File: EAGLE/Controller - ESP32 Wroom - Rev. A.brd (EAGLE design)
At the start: 29.5 x 33 mm, 30 parts, among them IC1 ESP32-S3-WROOM-1-N8R2, IC2 MPM3610GQV-P, IC3 CP2102N-A02-GQFN20R, J1 DF12NB_4.0_-40DP-0.5V_51_, J4 FSI-105-03-X-S, J8 -

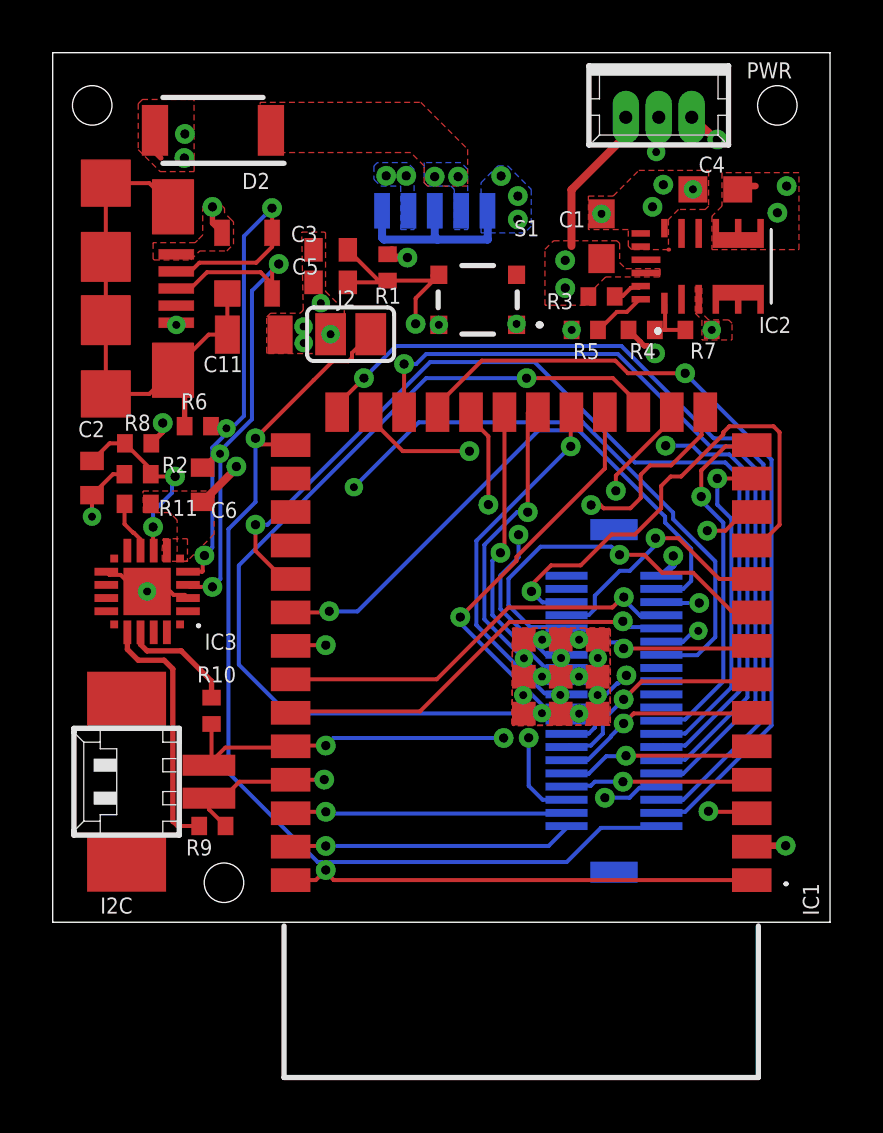
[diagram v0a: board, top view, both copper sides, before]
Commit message: Fixed some clearance error
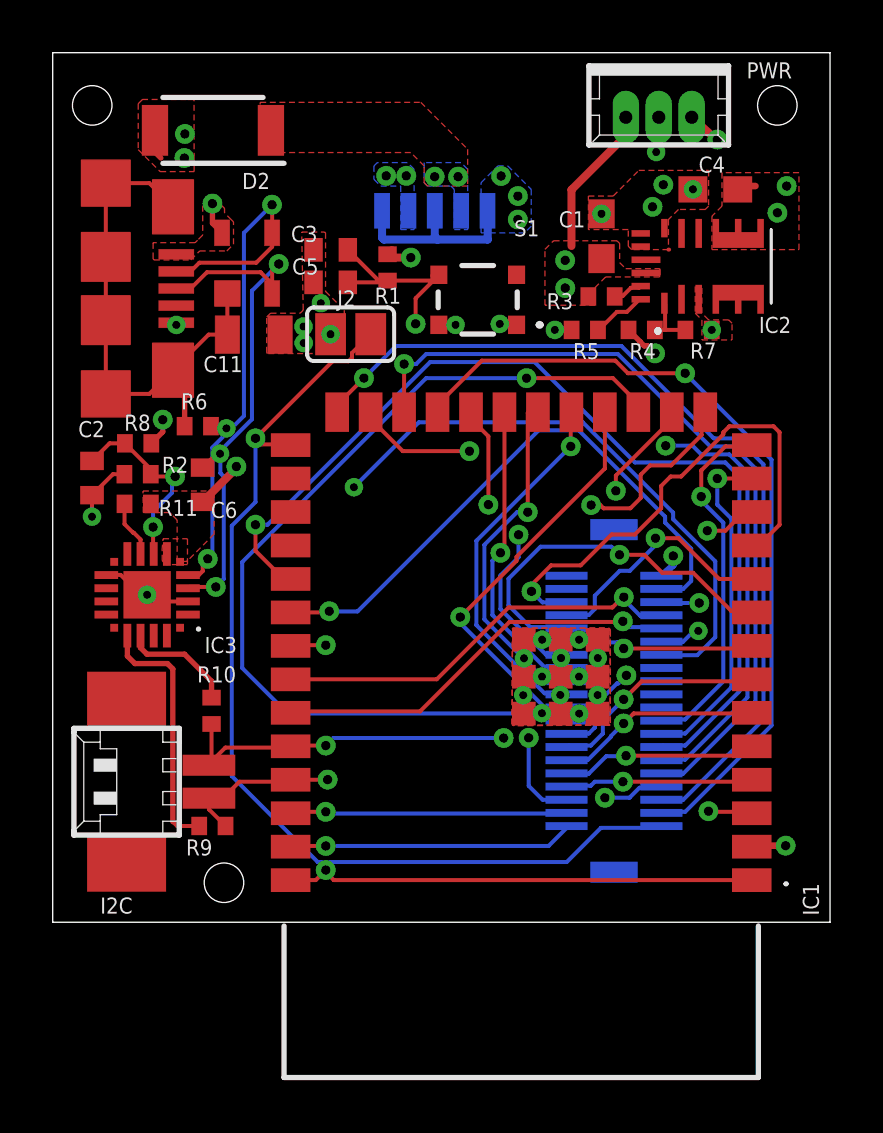
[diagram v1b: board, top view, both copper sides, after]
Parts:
- moved IC3 0.13 mm to (3.58, 12.4)
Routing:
- net GND: track 37.2 -> 39.0 mm

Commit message: Changed some via to be passthrought
Added schematic and new board layout prints
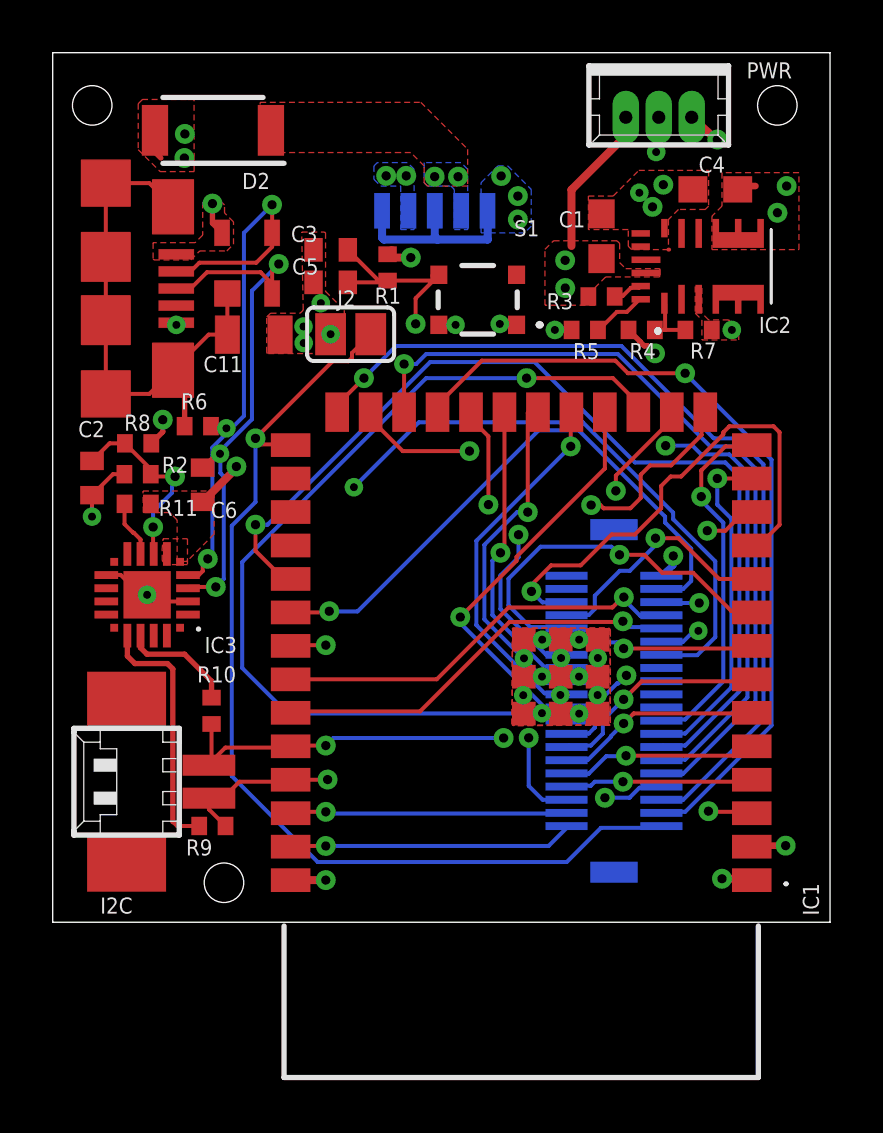
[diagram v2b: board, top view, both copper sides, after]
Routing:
- net GND: track 39.0 -> 23.7 mm
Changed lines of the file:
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@@
 <layer number="13" name="Route13" color="4" fill="5" visible="no" active="no"/>
 <layer number="14" name="Route14" color="1" fill="6" visible="no" active="no"/>
-<layer number="15" name="Route15" color="4" fill="6" visible="yes" active="yes"/>
+<layer number="15" name="Route15" color="4" fill="6" visible="no" active="yes"/>
 <layer number="16" name="Bottom" color="1" fill="1" visible="yes" active="yes"/>
 <layer number="17" name="Pads" color="2" fill="1" visible="yes" active="yes"/>
@@
 <layer number="43" name="vRestrict" color="2" fill="10" visible="no" active="yes"/>
 <layer number="44" name="Drills" color="7" fill="1" visible="no" active="yes"/>
-<layer number="45" name="Holes" color="7" fill="1" visible="yes" active="yes"/>
+<layer number="45" name="Holes" color="7" fill="1" visible="no" active="yes"/>
 <layer number="46" name="Milling" color="3" fill="1" visible="no" active="yes"/>
 <layer number="47" name="Measures" color="7" fill="1" visible="no" active="yes"/>
@@
 <param name="layerSetup" value="([2:1+(2*15)+16:15])"/>
 <param name="mtCopper" value="0.035mm 0.035mm 0.035mm 0.035mm 0.035mm 0.035mm 0.035mm 0.035mm 0.035mm 0.035mm 0.035mm 0.035mm 0.035mm 0.035mm 0.035mm 0.035mm"/>
-<param name="mtIsolate" value="0.11mm 1.6mm 0.2mm 0.15mm 0.2mm 0.15mm 0.2mm 0.15mm 0.2mm 0.15mm 0.2mm 0.15mm 0.2mm 0.15mm 0.11mm"/>
+<param name="mtIsolate" value="0.11mm 0.8mm 0.2mm 0.15mm 0.2mm 0.15mm 0.2mm 0.15mm 0.2mm 0.15mm 0.2mm 0.15mm 0.2mm 0.15mm 0.11mm"/>
 <param name="mdWireWire" value="6mil"/>
 <param name="mdWirePad" value="6mil"/>
@@
 <vertex x="24.638" y="22.86"/>
 <vertex x="24.638" y="22.098"/>
-<vertex x="25.781" y="22.098"/>
-<vertex x="25.781" y="22.733"/>
+<vertex x="26.035" y="22.098"/>
+<vertex x="26.035" y="22.479"/>
 <vertex x="25.654" y="22.86"/>
 <vertex x="24.892" y="22.86"/>
@@
 <wire x1="17.907" y1="10.5918" x2="17.88" y2="10.718" width="0.1524" layer="1"/>
 <wire x1="17.6784" y1="22.6314" x2="17.604" y2="22.672" width="0.1524" layer="1"/>
-<wire x1="9.9822" y1="1.6002" x2="9.0678" y2="1.6002" width="0.1524" layer="1"/>
-<wire x1="10.3632" y1="1.9812" x2="9.9822" y2="1.6002" width="0.1524" layer="1"/>
+<wire x1="10.3632" y1="1.6002" x2="9.0678" y2="1.6002" width="0.3048" layer="1"/>
 <wire x1="9.0678" y1="1.6002" x2="9.03" y2="1.598" width="0.1524" layer="1"/>
-<wire x1="10.668" y1="1.6002" x2="26.5176" y2="1.6002" width="0.1524" layer="1"/>
-<wire x1="10.3632" y1="1.905" x2="10.668" y2="1.6002" width="0.1524" layer="1"/>
-<wire x1="26.5176" y1="1.6002" x2="26.53" y2="1.598" width="0.1524" layer="1"/>
-<wire x1="10.3632" y1="1.905" x2="10.3632" y2="1.9812" width="0.1524" layer="1"/>
+<wire x1="26.53" y1="1.598" x2="26.5176" y2="1.6002" width="0.1524" layer="1"/>
+<wire x1="10.3632" y1="1.524" x2="10.3632" y2="1.6002" width="0.1524" layer="1"/>
 <wire x1="23.3934" y1="25.527" x2="23.368" y2="25.527" width="0.1524" layer="1"/>
-<via x="10.3632" y="1.9812" extent="1-2" drill="0.35"/>
+<via x="10.3632" y="1.6002" extent="1-16" drill="0.35"/>
 <wire x1="23.1" y1="13.15" x2="23.550659375" y2="13.546659375" width="0.254" layer="16"/>
 <wire x1="23.550659375" y1="13.546659375" x2="23.55064375" y2="13.90326875" width="0.254" layer="16"/>
@@
 <wire x1="17.88" y1="9.318" x2="17.8854" y2="9.318" width="0.254" layer="1"/>
 <wire x1="17.8854" y1="9.318" x2="17.907" y2="9.2964" width="0.254" layer="1"/>
-<via x="20.828" y="26.885" extent="1-2" drill="0.3" diameter="0.1778"/>
-<via x="24.296" y="27.813" extent="1-2" drill="0.3" diameter="0.1778"/>
+<via x="22.264" y="27.686" extent="1-2" drill="0.3" diameter="0.1778"/>
 <contactref element="PWR" pad="2"/>
 <wire x1="17.88" y1="10.718" x2="18.57040625" y2="10.718" width="0.1524" layer="1"/>
@@
 <via x="19.058" y="22.479" extent="1-2" drill="0.3"/>
 <via x="15.289" y="22.672" extent="1-2" drill="0.3"/>
-<via x="25.011" y="22.479" extent="1-2" drill="0.3"/>
+<via x="25.773" y="22.479" extent="1-2" drill="0.3"/>
 <wire x1="1.4915875" y1="16.2084875" x2="1.4915875" y2="15.393696875" width="0.1524" layer="1"/>
 <wire x1="1.4915875" y1="15.393696875" x2="1.4917625" y2="15.393521875" width="0.1524" layer="1"/>
@@
 <wire x1="14.654" y1="22.672" x2="15.289" y2="22.672" width="0.254" layer="1"/>
 <wire x1="19.693" y1="22.479" x2="19.058" y2="22.479" width="0.254" layer="1"/>
+<via x="25.4" y="1.651" extent="1-16" drill="0.35"/>
+<wire x1="26.5176" y1="1.6002" x2="26.4668" y2="1.651" width="0.3048" layer="1"/>
+<wire x1="26.4668" y1="1.651" x2="25.4" y2="1.651" width="0.3048" layer="1"/>
 </signal>
 <signal name="+3V3" class="2">
@@
 <via x="6.062571875" y="27.274003125" extent="1-16" drill="0.35"/>
 <polygon width="0.2032" layer="1" thermals="no">
-<vertex x="3.81" y="25.4"/>
+<vertex x="3.81" y="25.7817375"/>
 <vertex x="3.81" y="25.16705"/>
 <vertex x="3.841709375" y="25.135340625"/>
@@
 <vertex x="6.861625" y="25.729984375"/>
 <vertex x="6.861625" y="26.57851875"/>
-<vertex x="6.78813125" y="26.6520125"/>
 <vertex x="6.52088125" y="26.9192625"/>
-<vertex x="6.52088125" y="27.092984375"/>
-<vertex x="6.18013125" y="27.433734375"/>
-<vertex x="6.16009375" y="27.433734375"/>
-<vertex x="5.9329375" y="27.433734375"/>
-<vertex x="5.692409375" y="27.19320625"/>
+<vertex x="6.52088125" y="27.219984375"/>
+<vertex x="6.18013125" y="27.560734375"/>
+<vertex x="5.9329375" y="27.560734375"/>
+<vertex x="5.692409375" y="27.32020625"/>
 <vertex x="5.692409375" y="26.0774125"/>
-<vertex x="5.498653125" y="25.88365625"/>
 <vertex x="5.4051125" y="25.790115625"/>
 <vertex x="3.801621875" y="25.790115625"/>
-<vertex x="3.81" y="25.7817375"/>
 </polygon>
 <polygon width="0.2032" layer="1" thermals="no">
